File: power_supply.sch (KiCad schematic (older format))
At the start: 42 parts

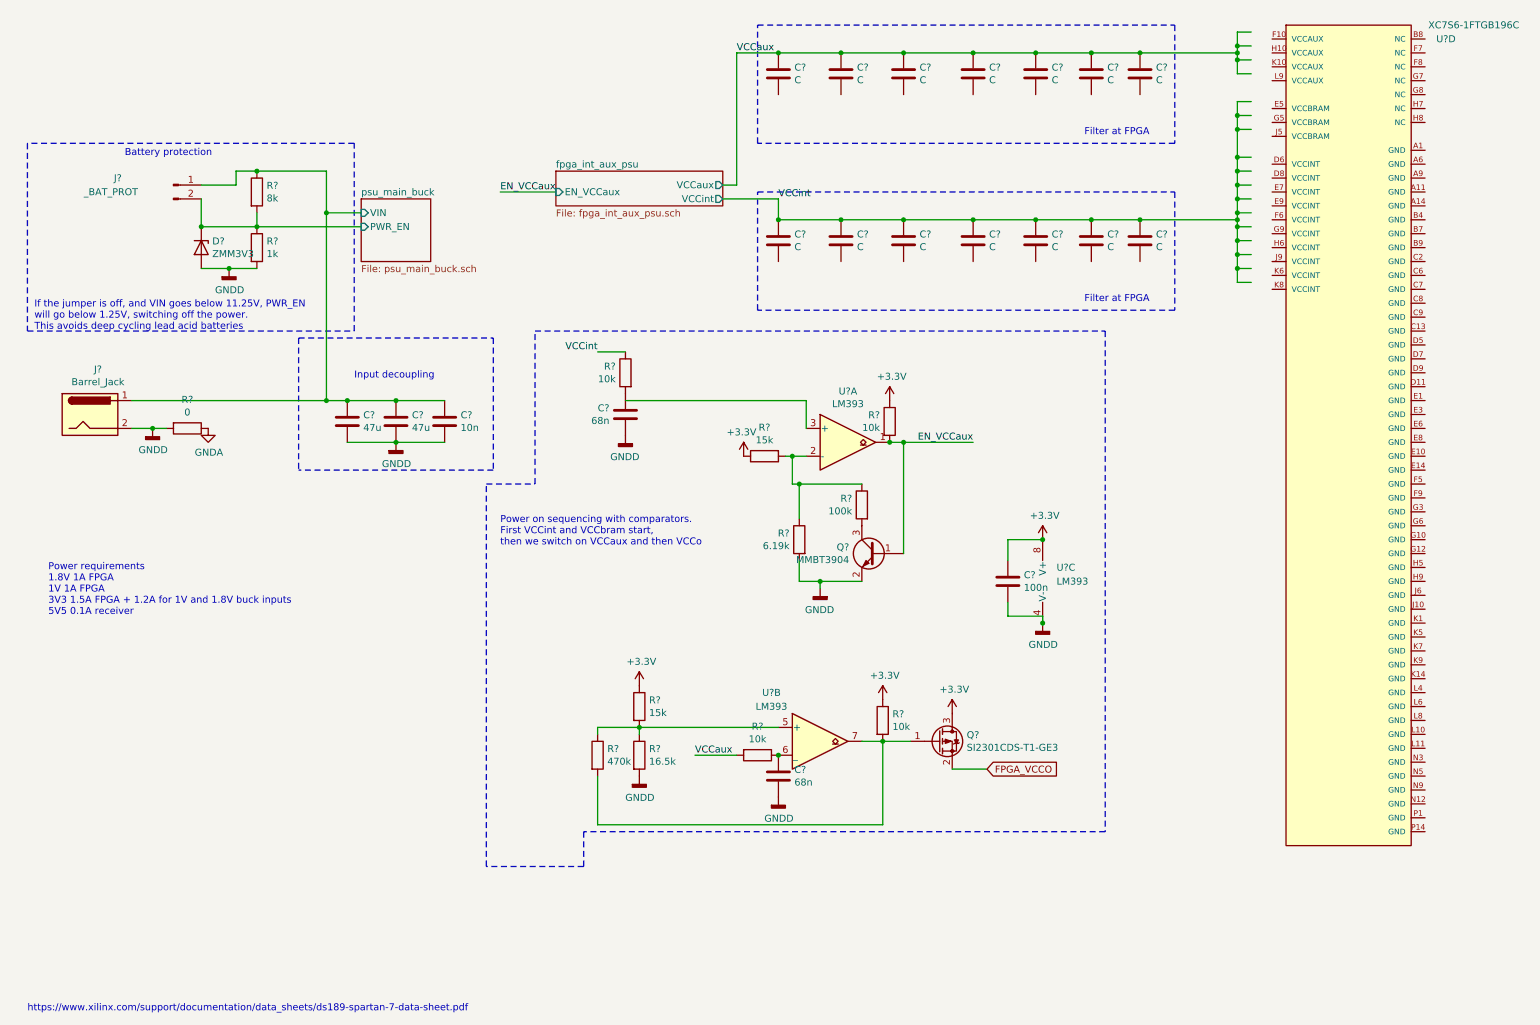
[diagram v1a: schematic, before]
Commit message: Power supply ,,typo" fixes
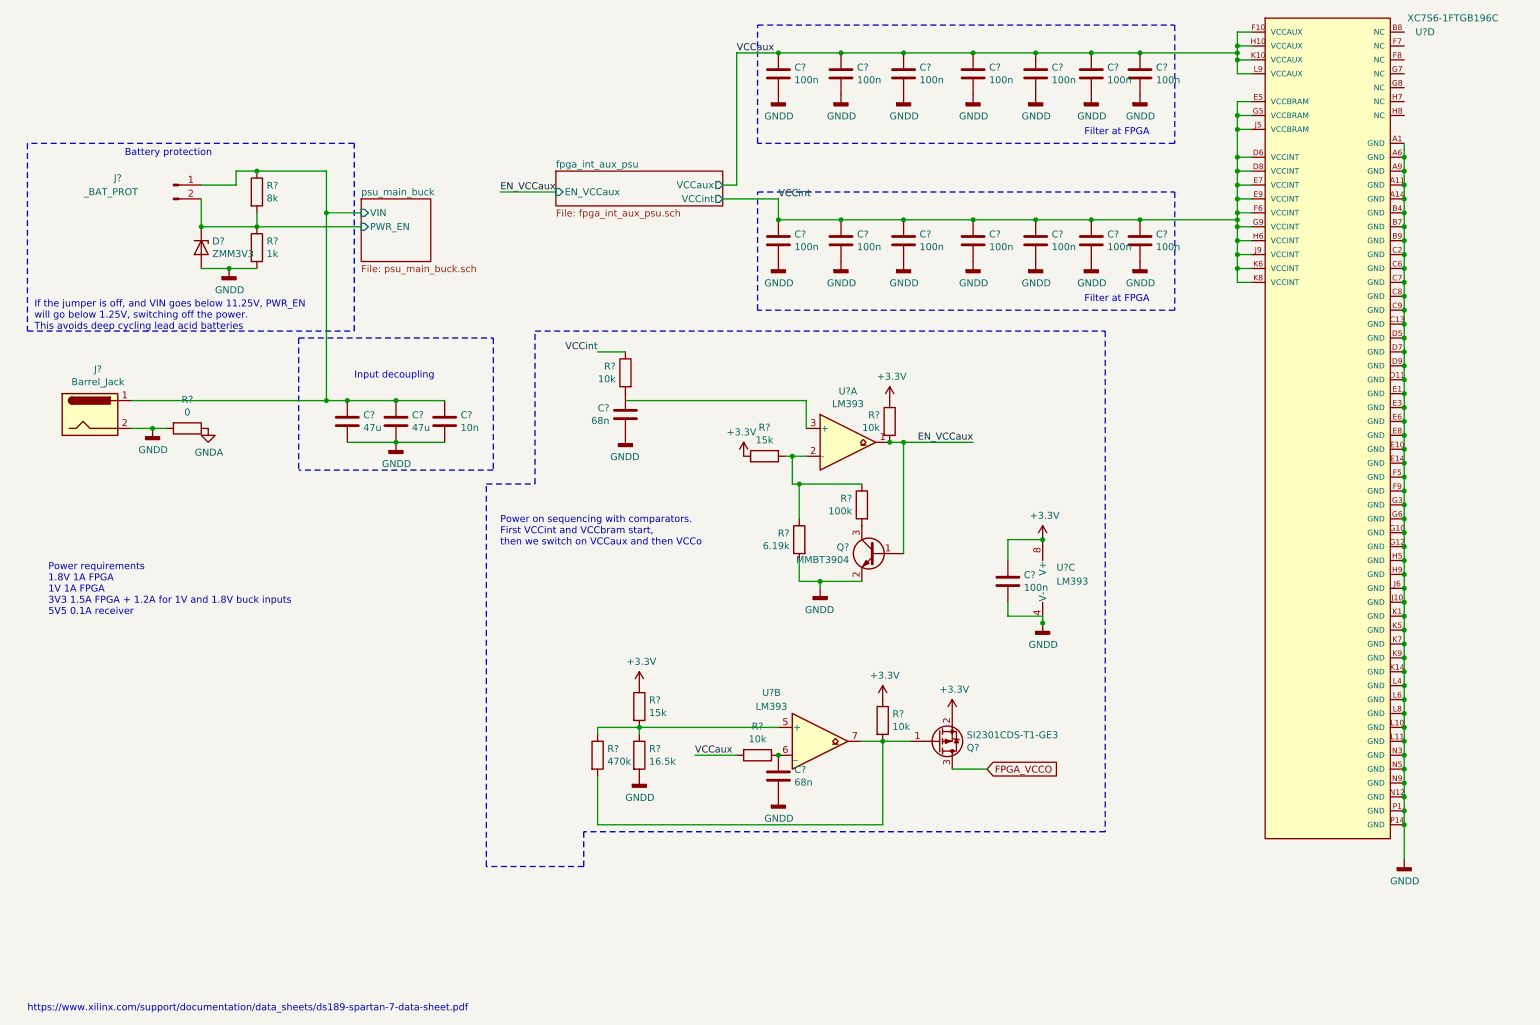
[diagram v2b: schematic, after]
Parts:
- C? (x14): value C -> 100n
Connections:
- wire segments 107 -> 157
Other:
- moved on the sheet: U?D

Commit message: Power suppley fixes
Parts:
- removed D?: ZMM3V3, symbol Device:D_Zener
- added C?: 470u, symbol Device:CP
- added C?: 47u, symbol Device:C
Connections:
- net FPGA_VCCO is gone; now on net +3V3: Q?.3 (D)
- net +3V3: no longer C?.1, Q?.2 (S), R?.1, R?.1, U?.8 (V+)
- net GNDD: now also J?.2 (Pin_2), C?.2, C?.2; no longer R?.2
- net psu_main_buck/VIN: now also C?.1, C?.1; no longer J?.1 (Pin_1)
- net psu_main_buck/PWR_EN renamed psu_main_buck/PWR_D_EN
- net psu_main_buck/PWR_D_EN: no longer J?.2 (Pin_2)
- new net: J?.1 (Pin_1), R?.2
- new net fpga_int_aux_psu/V_IN: C?.1, Q?.2 (S), R?.1, R?.1, U?.8 (V+)
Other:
- moved on the sheet: C?, J?

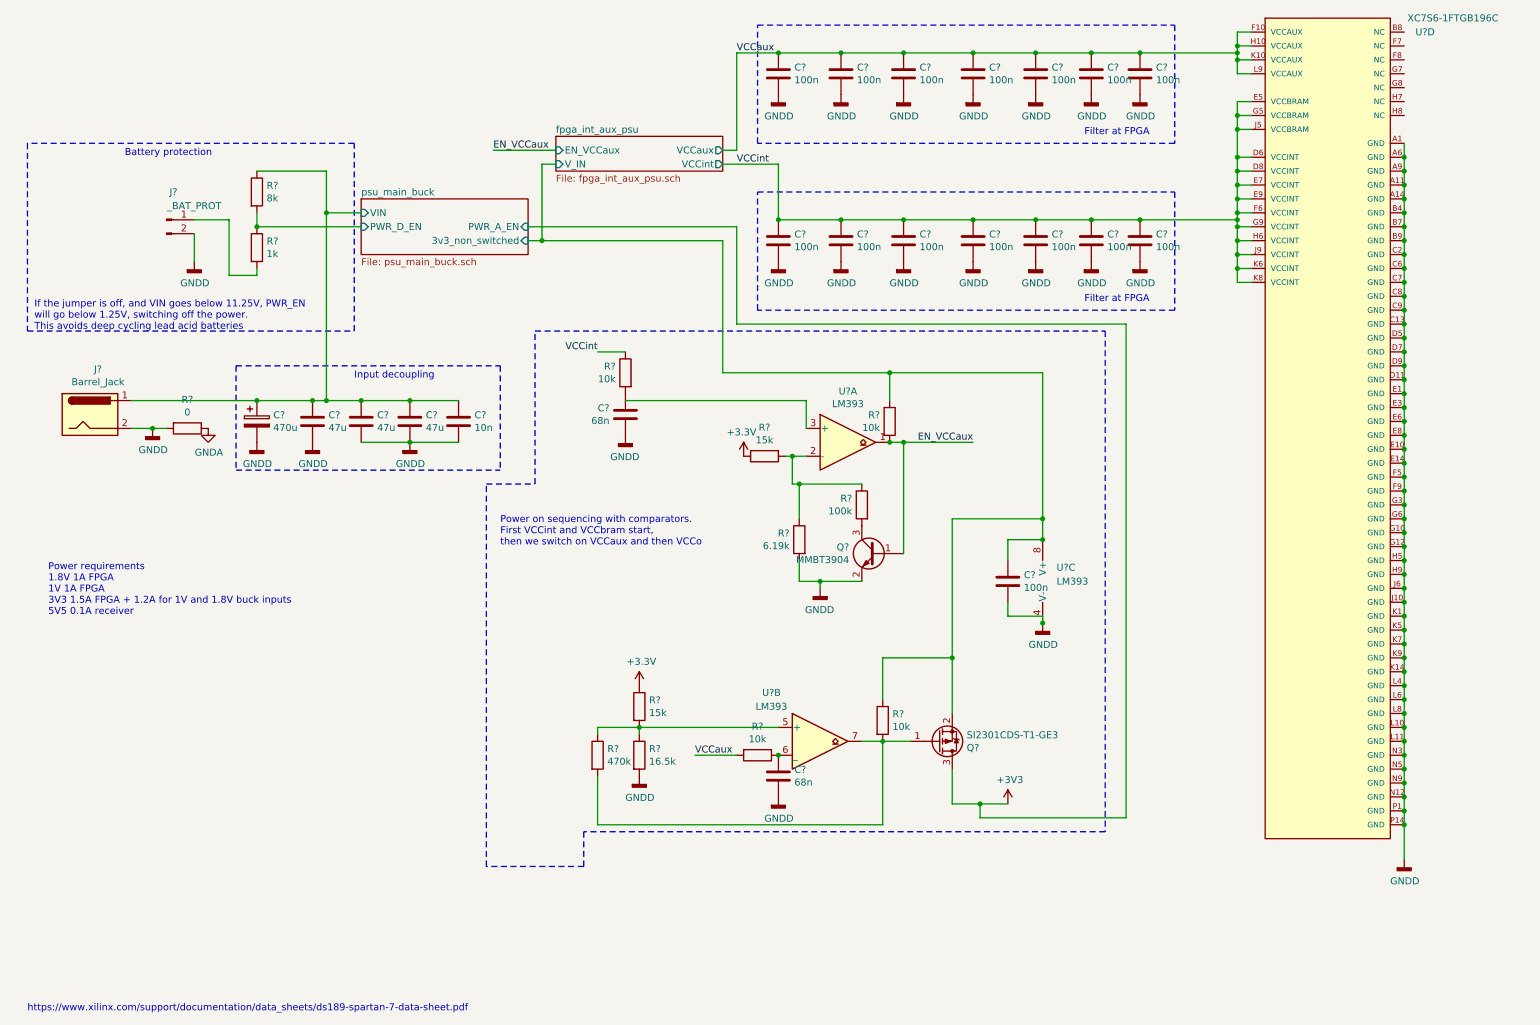
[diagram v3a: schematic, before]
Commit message: Add battery monitoring, and reverse polarity check
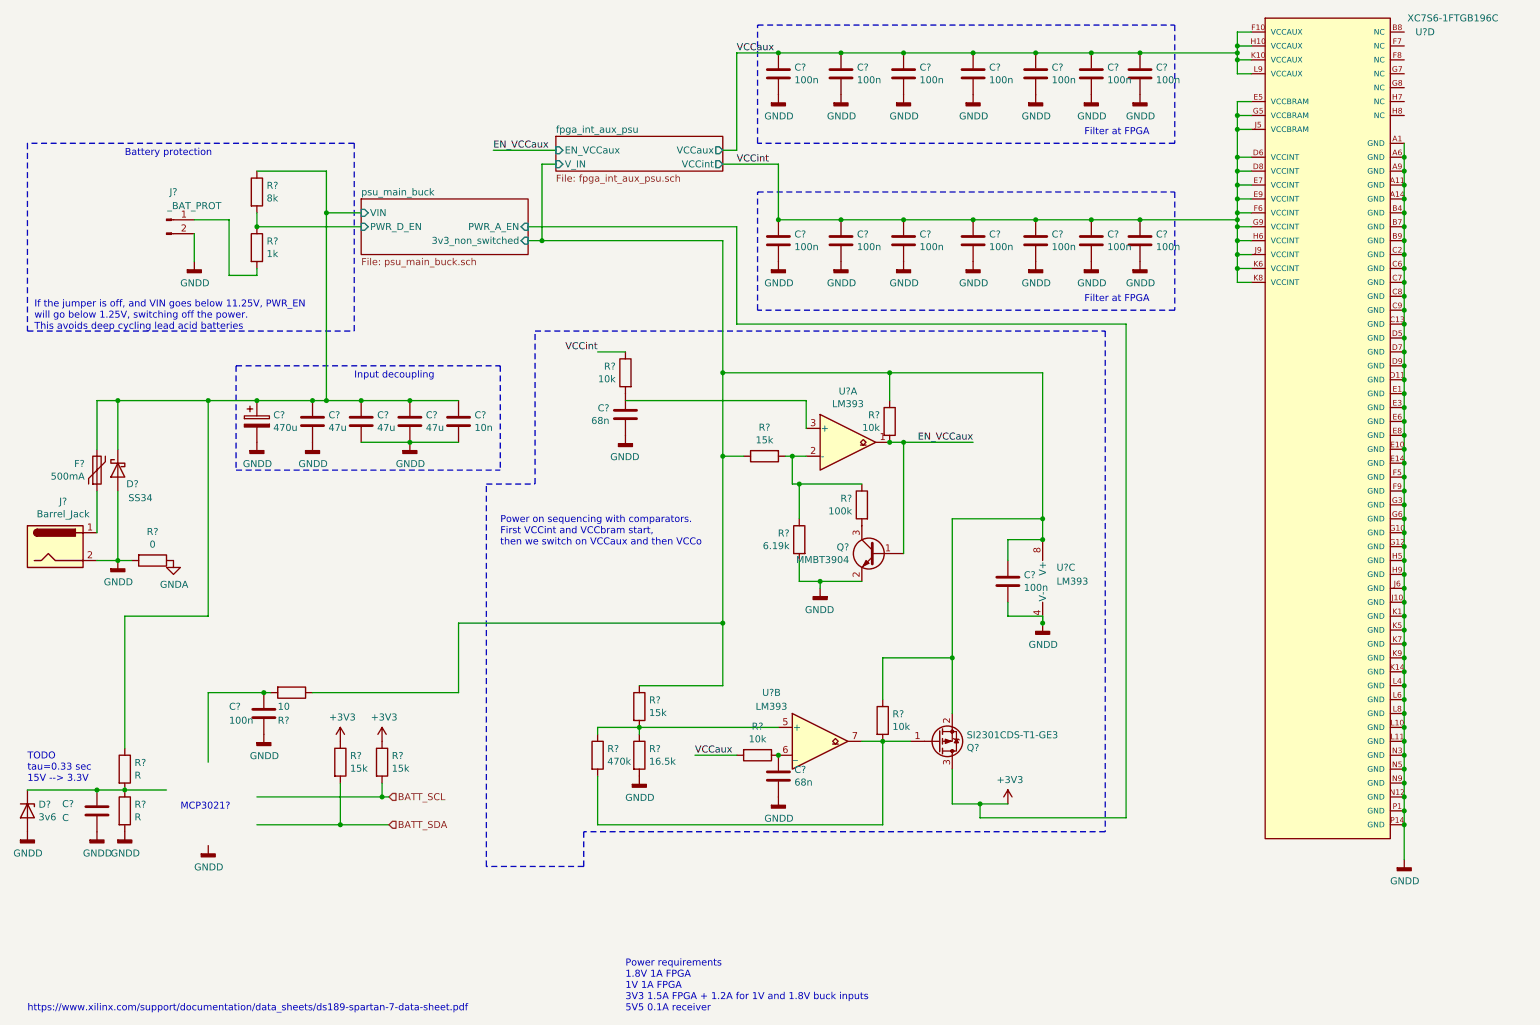
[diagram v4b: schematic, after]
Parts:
- added C?: 100n, symbol Device:C
- added C?: C, symbol Device:C
- added D?: SS34, symbol Device:D_Schottky
- added D?: 3v6, symbol Device:D_Zener
- added F?: 500mA, symbol Device:Polyfuse
- added R?: 10, symbol Device:R
- added R? (x2): 15k, symbol Device:R
- added R? (x2): R, symbol Device:R
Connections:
- net labels added: BATT_SCL, BATT_SDA
- net labels removed: +3.3V
- wire segments 180 -> 209
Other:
- note added: "MCP3021?"
- note added: "TODO\ntau=0.33 sec\n15V --> 3.3V"
- moved on the sheet: J?, R?

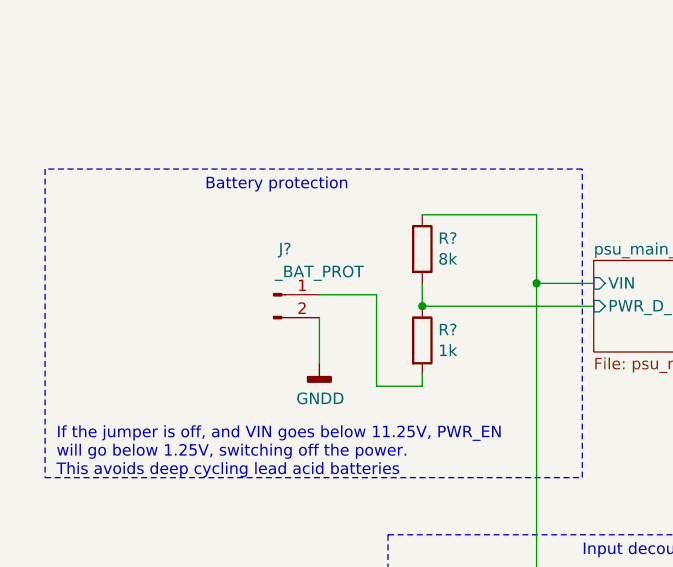
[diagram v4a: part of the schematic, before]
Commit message: Battery overdischarge jumper changed
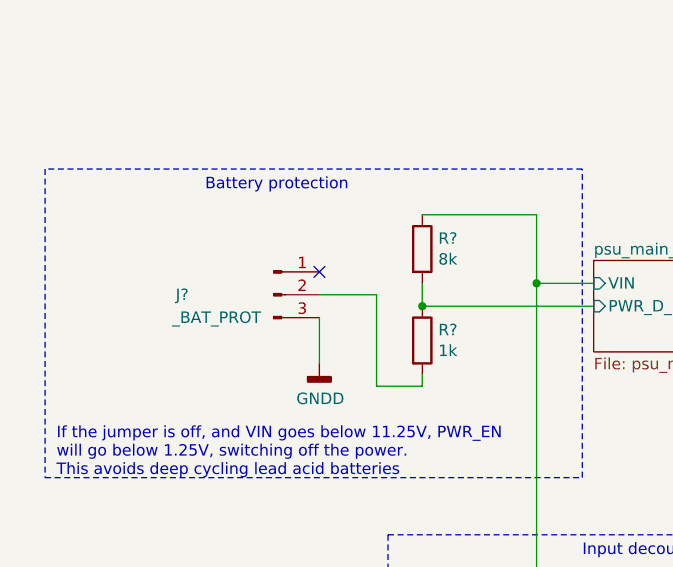
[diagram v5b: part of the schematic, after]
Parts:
- removed J?: _BAT_PROT, symbol Connector:Conn_01x02_Male
- added J?: _BAT_PROT, symbol Connector:Conn_01x03_Male
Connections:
- no-connect marks 0 -> 1
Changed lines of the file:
@@
-	1    0    0    -1
-$EndComp
-$Comp
-L Connector:Conn_01x02_Male J?
-U 1 1 603CF150
-P 1600 2000
-F 0 "J?" H 1650 2200 50  0000 C CNN
-F 1 "_BAT_PROT" H 1800 2100 50  0000 C CNN
-F 2 "" H 1600 2000 50  0001 C CNN
-F 3 "~" H 1600 2000 50  0001 C CNN
-	1    1600 2000
 	1    0    0    -1
 $EndComp
@@
 Wire Wire Line
 	1900 3300 2250 3300
+$Comp
+L Connector:Conn_01x03_Male J?
+U 1 1 60D41D02
+P 1600 2000
+F 0 "J?" H 1200 2000 50  0000 C CNN
+F 1 "_BAT_PROT" H 1350 1900 50  0000 C CNN
+F 2 "" H 1600 2000 50  0001 C CNN
+F 3 "~" H 1600 2000 50  0001 C CNN
+	1    1600 2000
+	1    0    0    -1
+$EndComp
+NoConn ~ 1800 1900
 $EndSCHEMATC

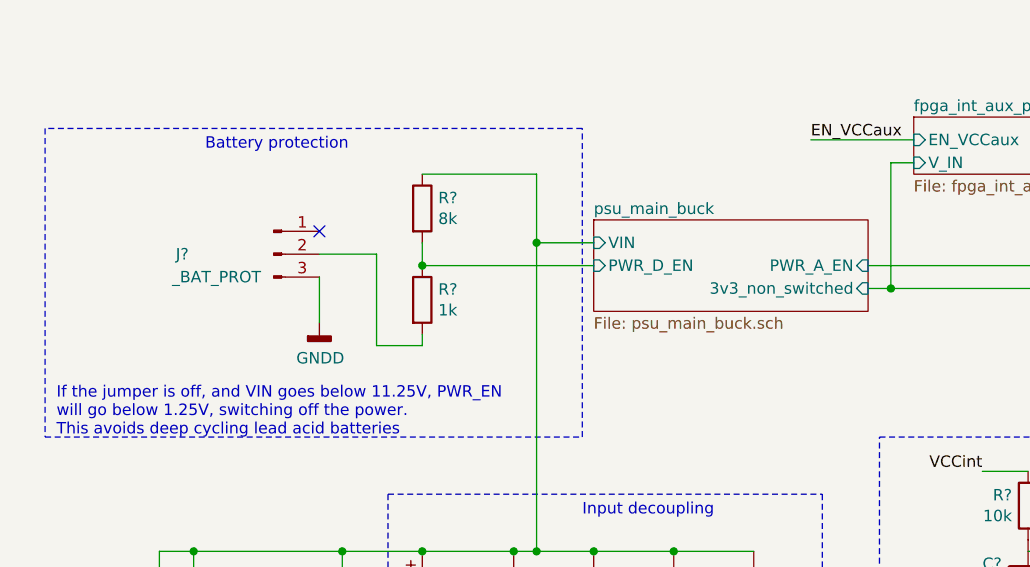
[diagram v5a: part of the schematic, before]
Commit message: fix battery protection jumper
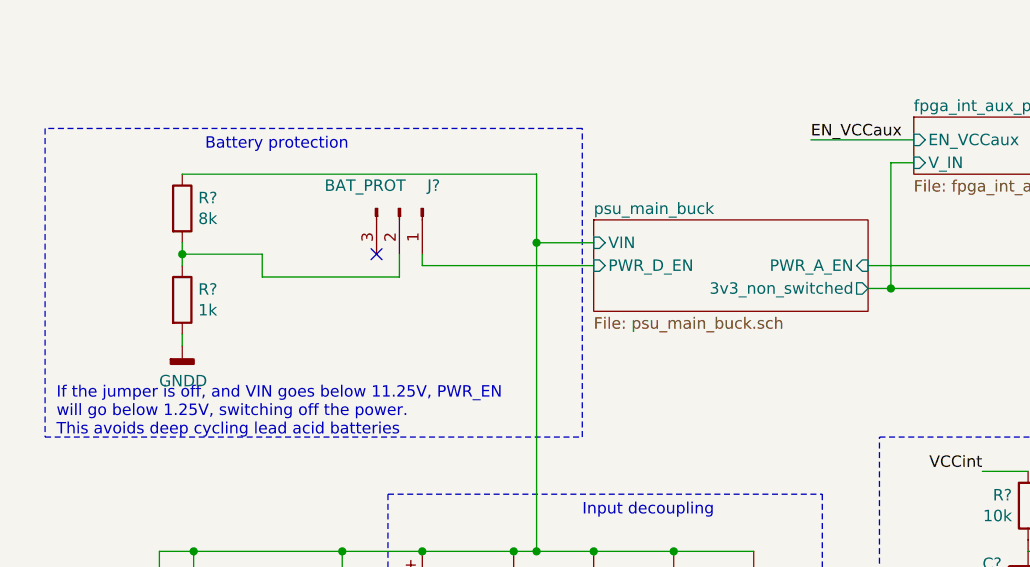
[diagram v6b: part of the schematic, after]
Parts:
- J?: value _BAT_PROT -> BAT_PROT
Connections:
- wire segments 209 -> 211
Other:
- moved on the sheet: J?, R?
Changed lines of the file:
@@
 L Device:R R?
 U 1 1 603CD7EC
-P 2250 1800
-F 0 "R?" H 2320 1846 50  0000 L CNN
-F 1 "8k" H 2320 1755 50  0000 L CNN
-F 2 "" V 2180 1800 50  0001 C CNN
-F 3 "~" H 2250 1800 50  0001 C CNN
-	1    2250 1800
+P 1200 1800
+F 0 "R?" H 1270 1846 50  0000 L CNN
+F 1 "8k" H 1270 1755 50  0000 L CNN
+F 2 "" V 1130 1800 50  0001 C CNN
+F 3 "~" H 1200 1800 50  0001 C CNN
+	1    1200 1800
 	1    0    0    -1
 $EndComp
@@
 L Device:R R?
 U 1 1 603CE2E9
-P 2250 2200
-F 0 "R?" H 2320 2246 50  0000 L CNN
-F 1 "1k" H 2320 2155 50  0000 L CNN
-F 2 "" V 2180 2200 50  0001 C CNN
-F 3 "~" H 2250 2200 50  0001 C CNN
-	1    2250 2200
-	1    0    0    -1
-$EndComp
-Wire Wire Line
-	1800 2000 2050 2000
-Wire Wire Line
-	2250 1950 2250 2050
-Connection ~ 2250 2050
-Wire Wire Line
-	1800 2100 1800 2300
-$Comp
-L power:GNDD #PWR?
-U 1 1 603EE0BE
-P 1800 2300
-AR Path="/603EE0BE" Ref="#PWR?"  Part="1"
-AR Path="/6004B3B4/603EE0BE" Ref="#PWR?"  Part="1"
-F 0 "#PWR?" H 1800 2050 50  0001 C CNN
-F 1 "GNDD" H 1804 2145 50  0000 C CNN
-F 2 "" H 1800 2300 50  0001 C CNN
-F 3 "" H 1800 2300 50  0001 C CNN
-	1    1800 2300
-	1    0    0    -1
-$EndComp
+P 1200 2200
+F 0 "R?" H 1270 2246 50  0000 L CNN
+F 1 "1k" H 1270 2155 50  0000 L CNN
+F 2 "" V 1130 2200 50  0001 C CNN
+F 3 "~" H 1200 2200 50  0001 C CNN
+	1    1200 2200
+	1    0    0    -1
+$EndComp
+Wire Wire Line
+	1200 1950 1200 2000
 $Comp
 L Device:C C?
@@
 F1 "psu_main_buck.sch" 50
 F2 "VIN" I L 3000 1950 50
-F3 "3v3_non_switched" I R 4200 2150 50
-F4 "PWR_D_EN" I L 3000 2050 50
-F5 "PWR_A_EN" I R 4200 2050 50
+F3 "PWR_D_EN" I L 3000 2050 50
+F4 "PWR_A_EN" I R 4200 2050 50
+F5 "3v3_non_switched" O R 4200 2150 50
 $EndSheet
 Connection ~ 2750 3300
 Wire Wire Line
 	2750 3300 3000 3300
-Wire Wire Line
-	2750 1650 2250 1650
 Wire Wire Line
 	2750 1650 2750 1950
@@
 	1    0    0    -1
 $EndComp
-Wire Wire Line
-	2250 2050 3000 2050
 Wire Wire Line
 	2750 1950 3000 1950
@@
 	2100 3050 4000 3050
 Wire Wire Line
-	2250 2350 2250 2400
-Wire Wire Line
-	2250 2400 2050 2400
-Wire Wire Line
-	2050 2400 2050 2000
+	1200 2350 1200 2400
 $Comp
 L power:GNDD #PWR?
@@
 L Connector:Conn_01x03_Male J?
 U 1 1 60D41D02
-P 1600 2000
-F 0 "J?" H 1200 2000 50  0000 C CNN
-F 1 "_BAT_PROT" H 1350 1900 50  0000 C CNN
-F 2 "" H 1600 2000 50  0001 C CNN
-F 3 "~" H 1600 2000 50  0001 C CNN
-	1    1600 2000
-	1    0    0    -1
-$EndComp
-NoConn ~ 1800 1900
+P 2150 1800
+F 0 "J?" V 2050 1950 50  0000 C CNN
+F 1 "BAT_PROT" V 2050 1650 50  0000 C CNN
+F 2 "" H 2150 1800 50  0001 C CNN
+F 3 "~" H 2150 1800 50  0001 C CNN
+	1    2150 1800
+	0    1    1    0
+$EndComp
+NoConn ~ 2050 2000
+$Comp
+L power:GNDD #PWR?
+U 1 1 60F18E22
+P 1200 2400
+F 0 "#PWR?" H 1200 2150 50  0001 C CNN
+F 1 "GNDD" H 1204 2245 50  0000 C CNN
+F 2 "" H 1200 2400 50  0001 C CNN
+F 3 "" H 1200 2400 50  0001 C CNN
+	1    1200 2400
+	1    0    0    -1
+$EndComp
+Wire Wire Line
+	2150 2000 2150 2100
+Wire Wire Line
+	2150 2100 1550 2100
+Wire Wire Line
+	1550 2100 1550 2000
+Wire Wire Line
+	1550 2000 1200 2000
+Connection ~ 1200 2000
+Wire Wire Line
+	1200 2000 1200 2050
+Wire Wire Line
+	2250 2000 2250 2050
+Wire Wire Line
+	2250 2050 3000 2050
+Wire Wire Line
+	1200 1650 2750 1650
 $EndSCHEMATC
